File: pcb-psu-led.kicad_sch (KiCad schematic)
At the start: 6 parts, among them J1 MAINS INPUT 230V, T1 Talema 70000K, U1 LM78L05ACZ

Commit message: PCB2-ECAD-01: add primary fuse F1
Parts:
- added F1: T32mA 250V, symbol PSU_LED:Fuse_5x20mm
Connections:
- net L_SW: now also F1.1; no longer T1.6 (P1_START)
- new net: F1.2, T1.6 (P1_START)
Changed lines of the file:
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@@
   (title_block
   (title "PCB PSU LED")
-  (rev "ECAD-11")
+  (rev "PCB2-ECAD-01")
   (company "Custom Step-Down PSU 230 V to 100 V")
-  (comment 1 "U1 LM78L05ACZ regulator added")
+  (comment 1 "F1 T32mA primary fuse added between L_SW and T1.6")
 )
   (wire
@@
   (wire
     (pts (xy 83.82 100.33) (xy 83.82 93.98))
-    (stroke
-      (width 0)
-      (type default)
-    )
-  )
-  (wire
-    (pts (xy 83.82 93.98) (xy 93.98 93.98))
     (stroke
       (width 0)
@@
           (unit 1)
         )
+      )
+    )
+  )
+  (symbol
+    (lib_id "PSU_LED:Fuse_5x20mm")
+    (at 88.9 93.98 0)
+    (unit 1)
+    (exclude_from_sim no)
+    (in_bom yes)
+    (on_board yes)
+    (dnp no)
+    (fields_autoplaced no)
+    (property "Reference" "F1"
+      (at 88.9 91.44 0)
+      (effects
+        (font (size 1.27 1.27))
+      )
+    )
+    (property "Value" "T32mA 250V"
+      (at 88.9 96.52 0)
+      (effects
+        (font (size 1.27 1.27))
+      )
+    )
+    (property "Footprint" ""
+      (at 88.9 93.98 0)
+      (effects
+        (font (size 1.27 1.27))
+        (hide yes)
+      )
+    )
+    (property "Datasheet" ""
+      (at 88.9 93.98 0)
+      (effects
+        (font (size 1.27 1.27))
+        (hide yes)
+      )
+    )
+    (property "Description" "Time-lag fuse, 32 mA, 250 V, 5x20 mm, primary protection for T1"
+      (at 88.9 93.98 0)
+      (effects
+        (font (size 1.27 1.27))
+        (hide yes)
+      )
+    )
+    (property "Manufacturer" "TBD"
+      (at 88.9 93.98 0)
+      (effects
+        (font (size 1.27 1.27))
+        (hide yes)
+      )
+    )
+    (property "MPN" "TBD"
+      (at 88.9 93.98 0)
+      (effects
+        (font (size 1.27 1.27))
+        (hide yes)
+      )
+    )
+    (pin "1"
+    )
+    (pin "2"
+    )
+    (instances
+      (project "pcb-psu-led"
+        (path "/a08e89e5-29a6-4ee5-b521-7a214388ab56"
+          (reference "F1")
+          (unit 1)
+        )

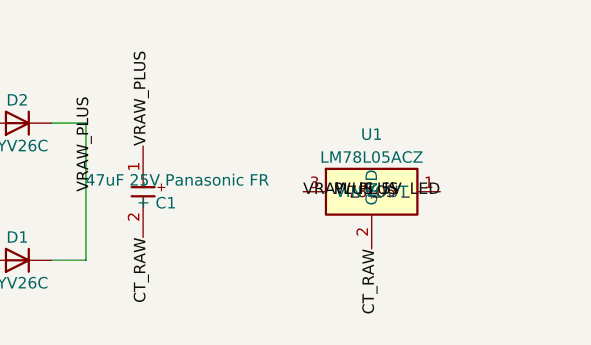
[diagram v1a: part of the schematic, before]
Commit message: PCB2-ECAD-02: add regulator decoupling capacitors
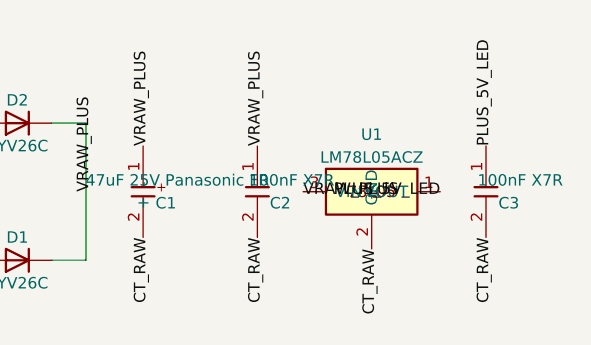
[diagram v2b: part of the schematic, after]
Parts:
- added C2, C3: 100nF X7R, symbol PSU_LED:C_Decoupling
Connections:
- net CT_RAW: now also C2.2, C3.2
- net PLUS_5V_LED: now also C3.1
- net VRAW_PLUS: now also C2.1
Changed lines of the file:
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@@
   (title_block
   (title "PCB PSU LED")
-  (rev "PCB2-ECAD-01")
+  (rev "PCB2-ECAD-02")
   (company "Custom Step-Down PSU 230 V to 100 V")
-  (comment 1 "F1 T32mA primary fuse added between L_SW and T1.6")
+  (comment 1 "C2 and C3 100nF X7R regulator decoupling added")
 )
   (wire
@@
   (label "PLUS_5V_LED"
     (at 167.64 101.6 180)
+    (effects
+      (font (size 1.27 1.27))
+    )
+  )
+  (label "VRAW_PLUS"
+    (at 147.32 96.52 90)
+    (effects
+      (font (size 1.27 1.27))
+    )
+  )
+  (label "CT_RAW"
+    (at 147.32 106.68 270)
+    (effects
+      (font (size 1.27 1.27))
+    )
+  )
+  (label "PLUS_5V_LED"
+    (at 172.72 96.52 90)
+    (effects
+      (font (size 1.27 1.27))
+    )
+  )
+  (label "CT_RAW"
+    (at 172.72 106.68 270)
     (effects
       (font (size 1.27 1.27))
@@
           (unit 1)
         )
+      )
+    )
+  )
+  (symbol
+    (lib_id "PSU_LED:C_Decoupling")
+    (at 147.32 101.6 0)
+    (unit 1)
+    (exclude_from_sim no)
+    (in_bom yes)
+    (on_board yes)
+    (dnp no)
+    (fields_autoplaced no)
+    (property "Reference" "C2"
+      (at 149.86 102.87 0)
+      (effects
+        (font (size 1.27 1.27))
+      )
+    )
+    (property "Value" "100nF X7R"
+      (at 151.13 100.33 0)
+      (effects
+        (font (size 1.27 1.27))
+      )
+    )
+    (property "Footprint" ""
+      (at 147.32 101.6 0)
+      (effects
+        (font (size 1.27 1.27))
+        (hide yes)
+      )
+    )
+    (property "Datasheet" ""
+      (at 147.32 101.6 0)
+      (effects
+        (font (size 1.27 1.27))
+        (hide yes)
+      )
+    )
+    (property "Description" "100 nF X7R THT local decoupling capacitor"
+      (at 147.32 101.6 0)
+      (effects
+        (font (size 1.27 1.27))
+        (hide yes)
+      )
+    )
+    (property "Manufacturer" "TBD"
+      (at 147.32 101.6 0)
+      (effects
+        (font (size 1.27 1.27))
+        (hide yes)
+      )
+    )
+    (property "MPN" "TBD"
+      (at 147.32 101.6 0)
+      (effects
+        (font (size 1.27 1.27))
+        (hide yes)
+      )
+    )
+    (pin "1"
+    )
+    (pin "2"
+    )
+    (instances
+      (project "pcb-psu-led"
+        (path "/a08e89e5-29a6-4ee5-b521-7a214388ab56"
+          (reference "C2")
+          (unit 1)
+        )
+      )
+    )
+  )
+  (symbol
+    (lib_id "PSU_LED:C_Decoupling")
+    (at 172.72 101.6 0)
+    (unit 1)
+    (exclude_from_sim no)
+    (in_bom yes)
+    (on_board yes)
+    (dnp no)
+    (fields_autoplaced no)
+    (property "Reference" "C3"
+      (at 175.26 102.87 0)
+      (effects
+        (font (size 1.27 1.27))
+      )
+    )
+    (property "Value" "100nF X7R"
+      (at 176.53 100.33 0)
+      (effects
+        (font (size 1.27 1.27))
+      )
+    )
+    (property "Footprint" ""
+      (at 172.72 101.6 0)
+      (effects
+        (font (size 1.27 1.27))
+        (hide yes)
+      )
+    )
+    (property "Datasheet" ""
+      (at 172.72 101.6 0)
+      (effects
+        (font (size 1.27 1.27))
+        (hide yes)
+      )
+    )
+    (property "Description" "100 nF X7R THT local decoupling capacitor"
+      (at 172.72 101.6 0)
+      (effects
+        (font (size 1.27 1.27))
+        (hide yes)
+      )
+    )
+    (property "Manufacturer" "TBD"
+      (at 172.72 101.6 0)
+      (effects
+        (font (size 1.27 1.27))
+        (hide yes)
+      )
+    )
+    (property "MPN" "TBD"
+      (at 172.72 101.6 0)
+      (effects
+        (font (size 1.27 1.27))
+        (hide yes)
+      )
+    )
+    (pin "1"
+    )
+    (pin "2"
+    )
+    (instances
+      (project "pcb-psu-led"
+        (path "/a08e89e5-29a6-4ee5-b521-7a214388ab56"
+          (reference "C3")
+          (unit 1)
+        )

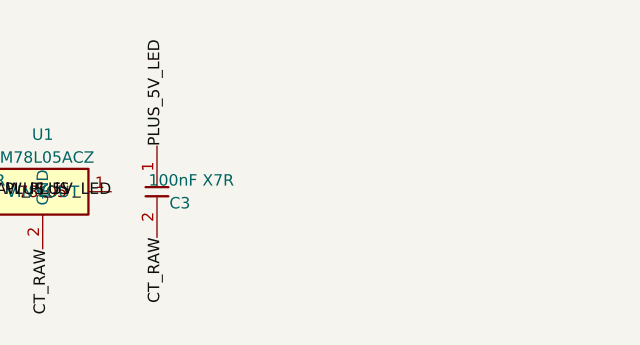
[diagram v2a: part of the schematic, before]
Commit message: PCB2-ECAD-03: add adjustable LED output stage
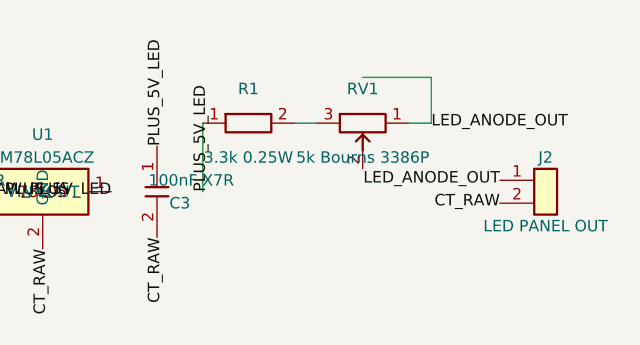
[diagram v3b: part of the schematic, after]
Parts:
- added J2: LED PANEL OUT, symbol PSU_LED:LED_Output_2Pin
- added R1: 3.3k 0.25W, symbol PSU_LED:R_Axial
- added RV1: 5k Bourns 3386P, symbol PSU_LED:RV_3386P
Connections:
- net CT_RAW: now also J2.2 (CATHODE)
- net PLUS_5V_LED: now also R1.1
- new net: R1.2, RV1.3 (CW)
- new net LED_ANODE_OUT: J2.1 (ANODE), RV1.1 (CCW)

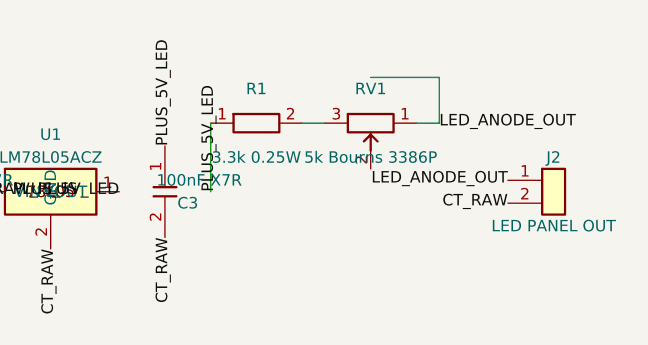
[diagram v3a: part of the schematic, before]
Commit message: PCB2-ECAD-03R1: connect RV1 wiper to output
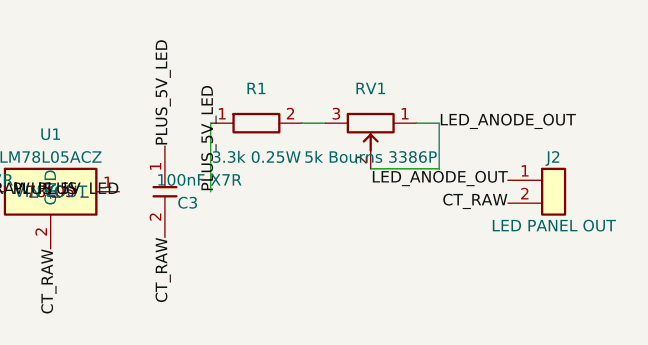
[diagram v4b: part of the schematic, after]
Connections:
- net LED_ANODE_OUT: now also RV1.2 (WIPER)
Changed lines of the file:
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@@
   (title_block
   (title "PCB PSU LED")
-  (rev "PCB2-ECAD-03")
+  (rev "PCB2-ECAD-03R1")
   (company "Custom Step-Down PSU 230 V to 100 V")
-  (comment 1 "R1, RV1 rheostat and J2 panel LED output added")
+  (comment 1 "RV1 wiper connected to output node")
 )
   (wire
@@
   )
   (wire
-    (pts (xy 195.58 88.9) (xy 203.2 88.9))
+    (pts (xy 195.58 99.06) (xy 203.2 99.06))
     (stroke (width 0) (type default))
   )
   (wire
-    (pts (xy 203.2 88.9) (xy 203.2 93.98))
+    (pts (xy 203.2 99.06) (xy 203.2 93.98))
     (stroke (width 0) (type default))
   )

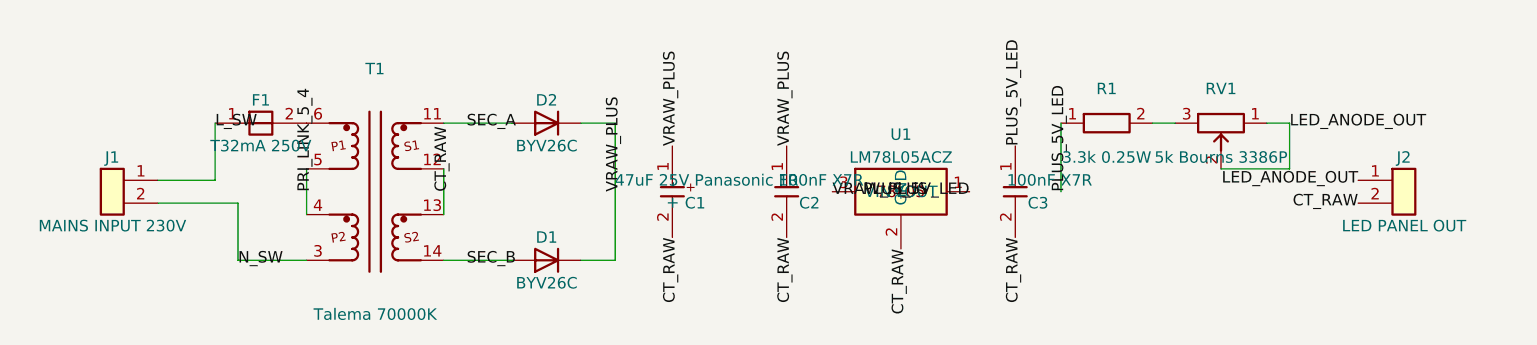
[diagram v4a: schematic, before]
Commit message: PCB2-ECAD-04: assign production footprints
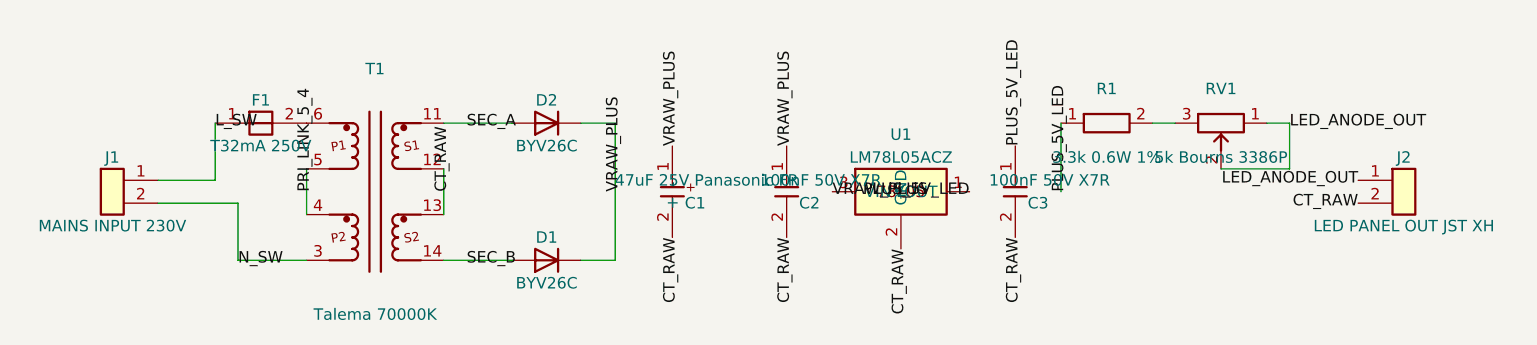
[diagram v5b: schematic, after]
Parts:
- C1: footprint (none) -> Capacitor_THT:CP_Radial_D5.0mm_P2.00mm; MPN EEU-FR1E470 -> EEUFR1E470
- C2, C3: value 100nF X7R -> 100nF 50V X7R; footprint (none) -> Capacitor_THT:C_Disc_D5.0mm_W2.5mm_P2.50mm; MPN TBD -> C315C104K5R5TA; Manufacturer TBD -> KEMET
- D1, D2: footprint (none) -> Diode_THT:D_DO-15_P10.16mm_Horizontal
- F1: footprint (none) -> Fuse:Fuseholder_Cylinder-5x20mm_Schurter_0031_8201_Horizontal_Open; MPN TBD -> 0031.8201; Manufacturer TBD -> Schurter
- J1: footprint (none) -> TerminalBlock_Phoenix:TerminalBlock_Phoenix_MKDS-1,5-2-5.08_1x02_P5.08mm_Horizontal; MPN TBD -> 1715721
- J2: value LED PANEL OUT -> LED PANEL OUT JST XH; footprint (none) -> Connector_JST:JST_XH_B2B-XH-A_1x02_P2.50mm_Vertical; MPN TBD -> B2B-XH-A(LF)(SN); Manufacturer TBD -> JST
- R1: value 3.3k 0.25W -> 3.3k 0.6W 1%; footprint (none) -> Resistor_THT:R_Axial_DIN0207_L6.3mm_D2.5mm_P10.16mm_Horizontal; MPN TBD -> MRS25000C3301FCT00; Manufacturer TBD -> Vishay
- RV1: footprint (none) -> Potentiometer_THT:Potentiometer_Bourns_3386P_Vertical
- U1: footprint (none) -> Package_TO_SOT_THT:TO-92_Inline; MPN LM78L05ACZ -> LM78L05ACZ/NOPB
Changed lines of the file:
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@@
   (title_block
   (title "PCB PSU LED")
-  (rev "PCB2-ECAD-03R1")
+  (rev "PCB2-ECAD-04")
   (company "Custom Step-Down PSU 230 V to 100 V")
-  (comment 1 "RV1 wiper connected to output node")
+  (comment 1 "Production footprints and exact mechanical parts assigned")
 )
   (wire
@@
       )
     )
-    (property "Footprint" ""
+    (property "Footprint" "TerminalBlock_Phoenix:TerminalBlock_Phoenix_MKDS-1,5-2-5.08_1x02_P5.08mm_Horizontal"
       (at 72.39 101.6 0)
       (effects
@@
       )
     )
-    (property "Datasheet" ""
+    (property "Datasheet" "https://www.phoenixcontact.com/en-pc/products/pcb-terminal-block-mkds-15-2-508-1715721"
       (at 72.39 101.6 0)
       (effects
@@
       )
     )
-    (property "Description" "2-pin mains input from NKK switch; exact Phoenix Contact part pending"
+    (property "Description" "Phoenix Contact MKDS 1,5/2-5,08 PCB terminal block, 2 positions, 5.08 mm pitch"
       (at 72.39 101.6 0)
       (effects
@@
       )
     )
-    (property "MPN" "TBD"
+    (property "MPN" "1715721"
       (at 72.39 101.6 0)
       (effects
@@
       )
     )
-    (property "Footprint" ""
+    (property "Footprint" "Fuse:Fuseholder_Cylinder-5x20mm_Schurter_0031_8201_Horizontal_Open"
       (at 88.9 93.98 0)
       (effects
@@
       )
     )
-    (property "Datasheet" ""
+    (property "Datasheet" "https://www.schurter.com/en/datasheet/typ_ogn.pdf"
       (at 88.9 93.98 0)
       (effects
@@
       )
     )
-    (property "Description" "Time-lag fuse, 32 mA, 250 V, 5x20 mm, primary protection for T1"
+    (property "Description" "Schurter OGN horizontal open PCB fuseholder for 5x20 mm fuse"
       (at 88.9 93.98 0)
       (effects
@@
       )
     )
-    (property "Manufacturer" "TBD"
+    (property "Manufacturer" "Schurter"
       (at 88.9 93.98 0)
       (effects
@@
       )
     )
-    (property "MPN" "TBD"
+    (property "MPN" "0031.8201"
       (at 88.9 93.98 0)
       (effects
@@
       (effects (font (size 1.27 1.27)))
     )
-    (property "Footprint" ""
+    (property "Footprint" "Diode_THT:D_DO-15_P10.16mm_Horizontal"
       (at 120.65 93.98 0)
       (effects
@@
       (effects (font (size 1.27 1.27)))
     )
-    (property "Footprint" ""
+    (property "Footprint" "Diode_THT:D_DO-15_P10.16mm_Horizontal"
       (at 120.65 109.22 0)
       (effects
@@
       )
     )
-    (property "Footprint" ""
+    (property "Footprint" "Package_TO_SOT_THT:TO-92_Inline"
       (at 160.02 101.6 0)
       (effects
@@
       )
     )
-    (property "Datasheet" ""
+    (property "Datasheet" "https://www.ti.com/lit/ds/symlink/lm78l.pdf"
       (at 160.02 101.6 0)
       (effects
@@
       )
     )
-    (property "MPN" "LM78L05ACZ"
+    (property "MPN" "LM78L05ACZ/NOPB"
       (at 160.02 101.6 0)
       (effects
@@
       )
     )
-    (property "Footprint" ""
+    (property "Footprint" "Capacitor_THT:CP_Radial_D5.0mm_P2.00mm"
       (at 134.62 101.6 0)
       (effects
@@
       )
     )
-    (property "Datasheet" ""
+    (property "Datasheet" "https://industrial.panasonic.com/ww/products/pt/aluminum-cap-lead/models/EEUFR1E470"
       (at 134.62 101.6 0)
       (effects
@@
       )
     )
-    (property "MPN" "EEU-FR1E470"
+    (property "MPN" "EEUFR1E470"
       (at 134.62 101.6 0)
       (effects
@@
       )
     )
-    (property "Value" "100nF X7R"
+    (property "Value" "100nF 50V X7R"
       (at 151.13 100.33 0)
       (effects
@@
       )
     )
-    (property "Footprint" ""
+    (property "Footprint" "Capacitor_THT:C_Disc_D5.0mm_W2.5mm_P2.50mm"
       (at 147.32 101.6 0)
       (effects
@@
       )
     )
-    (property "Datasheet" ""
+    (property "Datasheet" "https://yageogroup.com/download/specsheet/C315C104K5R5TA"
       (at 147.32 101.6 0)
       (effects
@@
       )
     )
-    (property "Description" "100 nF X7R THT local decoupling capacitor"
+    (property "Description" "KEMET GoldMax 100 nF, 50 V, X7R radial ceramic capacitor, 2.54 mm pitch"
       (at 147.32 101.6 0)
       (effects
@@
       )
     )
-    (property "Manufacturer" "TBD"
+    (property "Manufacturer" "KEMET"
       (at 147.32 101.6 0)
       (effects
@@
       )
     )
-    (property "MPN" "TBD"
+    (property "MPN" "C315C104K5R5TA"
       (at 147.32 101.6 0)
       (effects
@@
       )
     )
-    (property "Value" "100nF X7R"
+    (property "Value" "100nF 50V X7R"
       (at 176.53 100.33 0)
       (effects
@@
       )
     )
-    (property "Footprint" ""
+    (property "Footprint" "Capacitor_THT:C_Disc_D5.0mm_W2.5mm_P2.50mm"
       (at 172.72 101.6 0)
       (effects
@@
       )
     )
-    (property "Datasheet" ""
+    (property "Datasheet" "https://yageogroup.com/download/specsheet/C315C104K5R5TA"
       (at 172.72 101.6 0)
       (effects
@@
       )
     )
-    (property "Description" "100 nF X7R THT local decoupling capacitor"
+    (property "Description" "KEMET GoldMax 100 nF, 50 V, X7R radial ceramic capacitor, 2.54 mm pitch"
       (at 172.72 101.6 0)
       (effects
@@
       )
     )
-    (property "Manufacturer" "TBD"
+    (property "Manufacturer" "KEMET"
       (at 172.72 101.6 0)
       (effects
@@
       )
     )
-    (property "MPN" "TBD"
+    (property "MPN" "C315C104K5R5TA"
       (at 172.72 101.6 0)
       (effects
@@
       )
     )
-    (property "Value" "3.3k 0.25W"
+    (property "Value" "3.3k 0.6W 1%"
       (at 182.88 97.79 0)
       (effects
@@
       )
     )
-    (property "Footprint" ""
+    (property "Footprint" "Resistor_THT:R_Axial_DIN0207_L6.3mm_D2.5mm_P10.16mm_Horizontal"
       (at 182.88 93.98 0)
       (effects
@@
       )
     )
-    (property "Datasheet" ""
+    (property "Datasheet" "https://www.vishay.com/docs/28724/mrs16m25.pdf"
       (at 182.88 93.98 0)
       (effects
@@
       )
     )
-    (property "Description" "Fixed series current-limiting resistor for panel LED"
+    (property "Description" "Vishay MRS25 metal-film resistor, 3.3 kohm, 0.6 W, 1%"
       (at 182.88 93.98 0)
       (effects
@@
       )
     )
-    (property "Manufacturer" "TBD"
+    (property "Manufacturer" "Vishay"
       (at 182.88 93.98 0)
       (effects
@@
       )
     )
-    (property "MPN" "TBD"
+    (property "MPN" "MRS25000C3301FCT00"
       (at 182.88 93.98 0)
       (effects
@@
       )
     )
-    (property "Footprint" ""
+    (property "Footprint" "Potentiometer_THT:Potentiometer_Bourns_3386P_Vertical"
       (at 195.58 93.98 0)
       (effects
@@
       )
     )
-    (property "Value" "LED PANEL OUT"
+    (property "Value" "LED PANEL OUT JST XH"
       (at 215.9 105.41 0)
       (effects
@@
       )
     )
-    (property "Footprint" ""
+    (property "Footprint" "Connector_JST:JST_XH_B2B-XH-A_1x02_P2.50mm_Vertical"
       (at 215.9 101.6 0)
       (effects
@@
       )
     )
-    (property "Datasheet" ""
+    (property "Datasheet" "https://www.jst-mfg.com/product/pdf/eng/eXH.pdf"
       (at 215.9 101.6 0)
       (effects
@@
       )
     )
-    (property "Description" "Two-pin output connector to panel-mounted Kingbright WP7113ED LED; pin 1 anode, pin 2 cathode"
+    (property "Description" "JST XH 2-position vertical PCB header for panel LED wiring"
       (at 215.9 101.6 0)
       (effects
@@
       )
     )
-    (property "Manufacturer" "TBD"
+    (property "Manufacturer" "JST"
       (at 215.9 101.6 0)
       (effects
@@
       )
     )
-    (property "MPN" "TBD"
+    (property "MPN" "B2B-XH-A(LF)(SN)"
       (at 215.9 101.6 0)
       (effects

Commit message: PCB2-PCB-03R3: apply frozen footprints and clean DRC
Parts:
- F1: footprint Fuse:Fuseholder_Cylinder-5x20mm_Schurter_0031_8201_Horizontal_Open -> PSU_LED:Fuseholder_Cylinder-5x20mm_Schurter_0031_8201_Horizontal_Open
- J2: footprint Connector_JST:JST_XH_B2B-XH-A_1x02_P2.50mm_Vertical -> PSU_LED:JST_XH_B2B-XH-A_1x02_P2.50mm_Vertical
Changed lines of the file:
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@@
       )
     )
-    (property "Footprint" "Fuse:Fuseholder_Cylinder-5x20mm_Schurter_0031_8201_Horizontal_Open"
+    (property "Footprint" "PSU_LED:Fuseholder_Cylinder-5x20mm_Schurter_0031_8201_Horizontal_Open"
       (at 88.9 93.98 0)
       (effects
@@
       )
     )
-    (property "Footprint" "Connector_JST:JST_XH_B2B-XH-A_1x02_P2.50mm_Vertical"
+    (property "Footprint" "PSU_LED:JST_XH_B2B-XH-A_1x02_P2.50mm_Vertical"
       (at 215.9 101.6 0)
       (effects
